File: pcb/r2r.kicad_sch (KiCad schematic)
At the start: 8 parts

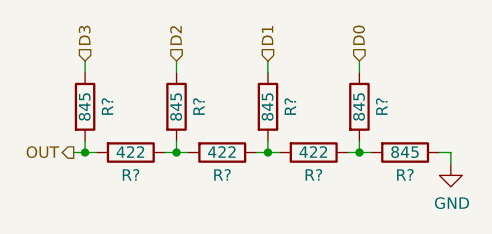
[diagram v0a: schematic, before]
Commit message: PCB: add reset circuit, xtal
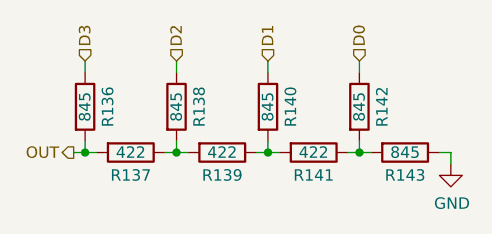
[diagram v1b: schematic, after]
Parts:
- gave numbers to parts that had none: 8
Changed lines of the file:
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@@
 (kicad_sch
-	(version 20231120)
+	(version 20250114)
 	(generator "eeschema")
-	(generator_version "8.0")
+	(generator_version "9.0")
 	(paper "A5")
 	(junction
@@
 		(on_board yes)
 		(dnp no)
-		(property "Reference" "#PWR?"
+		(property "Reference" "#PWR0413"
 			(at 127 71.12 0)
 			(effects
@@
 			(project "fnx51"
 				(path "/e63e39d7-6ac0-4ffd-8aa3-1841a4541b55/90e1f016-3c60-4383-aa8d-def9977ac47b/91068912-38bb-46cd-9b18-d1871085dfd0"
-					(reference "#PWR?")
+					(reference "#PWR0415")
 					(unit 1)
 				)
 				(path "/e63e39d7-6ac0-4ffd-8aa3-1841a4541b55/90e1f016-3c60-4383-aa8d-def9977ac47b/aa0b7daf-7acd-446b-bc05-f74af189bf7c"
-					(reference "#PWR?")
+					(reference "#PWR0414")
 					(unit 1)
 				)
 				(path "/e63e39d7-6ac0-4ffd-8aa3-1841a4541b55/90e1f016-3c60-4383-aa8d-def9977ac47b/dde75323-f81a-495f-a05e-373a126dd215"
-					(reference "#PWR?")
+					(reference "#PWR0413")
 					(unit 1)
 				)
@@
 		(on_board yes)
 		(dnp no)
-		(property "Reference" "R?"
+		(property "Reference" "R142"
 			(at 119.38 58.42 90)
 			(effects
@@
 			(project "fnx51"
 				(path "/e63e39d7-6ac0-4ffd-8aa3-1841a4541b55/90e1f016-3c60-4383-aa8d-def9977ac47b/91068912-38bb-46cd-9b18-d1871085dfd0"
-					(reference "R?")
+					(reference "R158")
 					(unit 1)
 				)
 				(path "/e63e39d7-6ac0-4ffd-8aa3-1841a4541b55/90e1f016-3c60-4383-aa8d-def9977ac47b/aa0b7daf-7acd-446b-bc05-f74af189bf7c"
-					(reference "R?")
+					(reference "R150")
 					(unit 1)
 				)
 				(path "/e63e39d7-6ac0-4ffd-8aa3-1841a4541b55/90e1f016-3c60-4383-aa8d-def9977ac47b/dde75323-f81a-495f-a05e-373a126dd215"
-					(reference "R?")
+					(reference "R142")
 					(unit 1)
 				)
@@
 		(on_board yes)
 		(dnp no)
-		(property "Reference" "R?"
+		(property "Reference" "R138"
 			(at 99.06 58.42 90)
 			(effects
@@
 			(project "fnx51"
 				(path "/e63e39d7-6ac0-4ffd-8aa3-1841a4541b55/90e1f016-3c60-4383-aa8d-def9977ac47b/91068912-38bb-46cd-9b18-d1871085dfd0"
-					(reference "R?")
+					(reference "R154")
 					(unit 1)
 				)
 				(path "/e63e39d7-6ac0-4ffd-8aa3-1841a4541b55/90e1f016-3c60-4383-aa8d-def9977ac47b/aa0b7daf-7acd-446b-bc05-f74af189bf7c"
-					(reference "R?")
+					(reference "R146")
 					(unit 1)
 				)
 				(path "/e63e39d7-6ac0-4ffd-8aa3-1841a4541b55/90e1f016-3c60-4383-aa8d-def9977ac47b/dde75323-f81a-495f-a05e-373a126dd215"
-					(reference "R?")
+					(reference "R138")
 					(unit 1)
 				)
@@
 		(on_board yes)
 		(dnp no)
-		(property "Reference" "R?"
+		(property "Reference" "R139"
 			(at 101.6 66.04 90)
 			(effects
@@
 			(project "fnx51"
 				(path "/e63e39d7-6ac0-4ffd-8aa3-1841a4541b55/90e1f016-3c60-4383-aa8d-def9977ac47b/91068912-38bb-46cd-9b18-d1871085dfd0"
-					(reference "R?")
+					(reference "R155")
 					(unit 1)
 				)
 				(path "/e63e39d7-6ac0-4ffd-8aa3-1841a4541b55/90e1f016-3c60-4383-aa8d-def9977ac47b/aa0b7daf-7acd-446b-bc05-f74af189bf7c"
-					(reference "R?")
+					(reference "R147")
 					(unit 1)
 				)
 				(path "/e63e39d7-6ac0-4ffd-8aa3-1841a4541b55/90e1f016-3c60-4383-aa8d-def9977ac47b/dde75323-f81a-495f-a05e-373a126dd215"
-					(reference "R?")
+					(reference "R139")
 					(unit 1)
 				)
@@
 		(on_board yes)
 		(dnp no)
-		(property "Reference" "R?"
+		(property "Reference" "R140"
 			(at 109.22 58.42 90)
 			(effects
@@
 			(project "fnx51"
 				(path "/e63e39d7-6ac0-4ffd-8aa3-1841a4541b55/90e1f016-3c60-4383-aa8d-def9977ac47b/91068912-38bb-46cd-9b18-d1871085dfd0"
-					(reference "R?")
+					(reference "R156")
 					(unit 1)
 				)
 				(path "/e63e39d7-6ac0-4ffd-8aa3-1841a4541b55/90e1f016-3c60-4383-aa8d-def9977ac47b/aa0b7daf-7acd-446b-bc05-f74af189bf7c"
-					(reference "R?")
+					(reference "R148")
 					(unit 1)
 				)
 				(path "/e63e39d7-6ac0-4ffd-8aa3-1841a4541b55/90e1f016-3c60-4383-aa8d-def9977ac47b/dde75323-f81a-495f-a05e-373a126dd215"
-					(reference "R?")
+					(reference "R140")
 					(unit 1)
 				)
@@
 		(on_board yes)
 		(dnp no)
-		(property "Reference" "R?"
+		(property "Reference" "R143"
 			(at 121.92 66.04 90)
 			(effects
@@
 			(project "fnx51"
 				(path "/e63e39d7-6ac0-4ffd-8aa3-1841a4541b55/90e1f016-3c60-4383-aa8d-def9977ac47b/91068912-38bb-46cd-9b18-d1871085dfd0"
-					(reference "R?")
+					(reference "R159")
 					(unit 1)
 				)
 				(path "/e63e39d7-6ac0-4ffd-8aa3-1841a4541b55/90e1f016-3c60-4383-aa8d-def9977ac47b/aa0b7daf-7acd-446b-bc05-f74af189bf7c"
-					(reference "R?")
+					(reference "R151")
 					(unit 1)
 				)
 				(path "/e63e39d7-6ac0-4ffd-8aa3-1841a4541b55/90e1f016-3c60-4383-aa8d-def9977ac47b/dde75323-f81a-495f-a05e-373a126dd215"
-					(reference "R?")
+					(reference "R143")
 					(unit 1)
 				)
@@
 		(on_board yes)
 		(dnp no)
-		(property "Reference" "R?"
+		(property "Reference" "R137"
 			(at 91.44 66.04 90)
 			(effects
@@
 			(project "fnx51"
 				(path "/e63e39d7-6ac0-4ffd-8aa3-1841a4541b55/90e1f016-3c60-4383-aa8d-def9977ac47b/91068912-38bb-46cd-9b18-d1871085dfd0"
-					(reference "R?")
+					(reference "R153")
 					(unit 1)
 				)
 				(path "/e63e39d7-6ac0-4ffd-8aa3-1841a4541b55/90e1f016-3c60-4383-aa8d-def9977ac47b/aa0b7daf-7acd-446b-bc05-f74af189bf7c"
-					(reference "R?")
+					(reference "R145")
 					(unit 1)
 				)
 				(path "/e63e39d7-6ac0-4ffd-8aa3-1841a4541b55/90e1f016-3c60-4383-aa8d-def9977ac47b/dde75323-f81a-495f-a05e-373a126dd215"
-					(reference "R?")
+					(reference "R137")
 					(unit 1)
 				)
@@
 		(on_board yes)
 		(dnp no)
-		(property "Reference" "R?"
+		(property "Reference" "R141"
 			(at 111.76 66.04 90)
 			(effects
@@
 			(project "fnx51"
 				(path "/e63e39d7-6ac0-4ffd-8aa3-1841a4541b55/90e1f016-3c60-4383-aa8d-def9977ac47b/91068912-38bb-46cd-9b18-d1871085dfd0"
-					(reference "R?")
+					(reference "R157")
 					(unit 1)
 				)
 				(path "/e63e39d7-6ac0-4ffd-8aa3-1841a4541b55/90e1f016-3c60-4383-aa8d-def9977ac47b/aa0b7daf-7acd-446b-bc05-f74af189bf7c"
-					(reference "R?")
+					(reference "R149")
 					(unit 1)
 				)
 				(path "/e63e39d7-6ac0-4ffd-8aa3-1841a4541b55/90e1f016-3c60-4383-aa8d-def9977ac47b/dde75323-f81a-495f-a05e-373a126dd215"
-					(reference "R?")
+					(reference "R141")
 					(unit 1)
 				)
@@
 		(on_board yes)
 		(dnp no)
-		(property "Reference" "R?"
+		(property "Reference" "R136"
 			(at 88.9 58.42 90)
 			(effects
@@
 			(project "fnx51"
 				(path "/e63e39d7-6ac0-4ffd-8aa3-1841a4541b55/90e1f016-3c60-4383-aa8d-def9977ac47b/91068912-38bb-46cd-9b18-d1871085dfd0"
-					(reference "R?")
+					(reference "R152")
 					(unit 1)
 				)
 				(path "/e63e39d7-6ac0-4ffd-8aa3-1841a4541b55/90e1f016-3c60-4383-aa8d-def9977ac47b/aa0b7daf-7acd-446b-bc05-f74af189bf7c"
-					(reference "R?")
+					(reference "R144")
 					(unit 1)
 				)
 				(path "/e63e39d7-6ac0-4ffd-8aa3-1841a4541b55/90e1f016-3c60-4383-aa8d-def9977ac47b/dde75323-f81a-495f-a05e-373a126dd215"
-					(reference "R?")
-					(unit 1)
-				)
+					(reference "R136")
+					(unit 1)
+				)

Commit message: WIP schematic
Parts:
- renumbered R136 to R143, R137 to R144, R138 to R145, R139 to R146, R140 to R147, R141 to R148, R142 to R149, R143 to R150
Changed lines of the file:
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@@
 		(on_board yes)
 		(dnp no)
-		(property "Reference" "#PWR0413"
+		(property "Reference" "#PWR0430"
 			(at 127 71.12 0)
 			(effects
@@
 			(project "fnx51"
 				(path "/e63e39d7-6ac0-4ffd-8aa3-1841a4541b55/90e1f016-3c60-4383-aa8d-def9977ac47b/91068912-38bb-46cd-9b18-d1871085dfd0"
-					(reference "#PWR0415")
-					(unit 1)
-				)
-				(path "/e63e39d7-6ac0-4ffd-8aa3-1841a4541b55/90e1f016-3c60-4383-aa8d-def9977ac47b/aa0b7daf-7acd-446b-bc05-f74af189bf7c"
-					(reference "#PWR0414")
-					(unit 1)
-				)
-				(path "/e63e39d7-6ac0-4ffd-8aa3-1841a4541b55/90e1f016-3c60-4383-aa8d-def9977ac47b/dde75323-f81a-495f-a05e-373a126dd215"
-					(reference "#PWR0413")
+					(reference "#PWR0432")
+					(unit 1)
+				)
+				(path "/e63e39d7-6ac0-4ffd-8aa3-1841a4541b55/90e1f016-3c60-4383-aa8d-def9977ac47b/aa0b7daf-7acd-446b-bc05-f74af189bf7c"
+					(reference "#PWR0431")
+					(unit 1)
+				)
+				(path "/e63e39d7-6ac0-4ffd-8aa3-1841a4541b55/90e1f016-3c60-4383-aa8d-def9977ac47b/dde75323-f81a-495f-a05e-373a126dd215"
+					(reference "#PWR0430")
 					(unit 1)
 				)
@@
 		(on_board yes)
 		(dnp no)
-		(property "Reference" "R142"
+		(property "Reference" "R149"
 			(at 119.38 58.42 90)
 			(effects
@@
 			(project "fnx51"
 				(path "/e63e39d7-6ac0-4ffd-8aa3-1841a4541b55/90e1f016-3c60-4383-aa8d-def9977ac47b/91068912-38bb-46cd-9b18-d1871085dfd0"
-					(reference "R158")
-					(unit 1)
-				)
-				(path "/e63e39d7-6ac0-4ffd-8aa3-1841a4541b55/90e1f016-3c60-4383-aa8d-def9977ac47b/aa0b7daf-7acd-446b-bc05-f74af189bf7c"
-					(reference "R150")
-					(unit 1)
-				)
-				(path "/e63e39d7-6ac0-4ffd-8aa3-1841a4541b55/90e1f016-3c60-4383-aa8d-def9977ac47b/dde75323-f81a-495f-a05e-373a126dd215"
-					(reference "R142")
+					(reference "R165")
+					(unit 1)
+				)
+				(path "/e63e39d7-6ac0-4ffd-8aa3-1841a4541b55/90e1f016-3c60-4383-aa8d-def9977ac47b/aa0b7daf-7acd-446b-bc05-f74af189bf7c"
+					(reference "R157")
+					(unit 1)
+				)
+				(path "/e63e39d7-6ac0-4ffd-8aa3-1841a4541b55/90e1f016-3c60-4383-aa8d-def9977ac47b/dde75323-f81a-495f-a05e-373a126dd215"
+					(reference "R149")
 					(unit 1)
 				)
@@
 		(on_board yes)
 		(dnp no)
-		(property "Reference" "R138"
+		(property "Reference" "R145"
 			(at 99.06 58.42 90)
 			(effects
@@
 			(project "fnx51"
 				(path "/e63e39d7-6ac0-4ffd-8aa3-1841a4541b55/90e1f016-3c60-4383-aa8d-def9977ac47b/91068912-38bb-46cd-9b18-d1871085dfd0"
-					(reference "R154")
-					(unit 1)
-				)
-				(path "/e63e39d7-6ac0-4ffd-8aa3-1841a4541b55/90e1f016-3c60-4383-aa8d-def9977ac47b/aa0b7daf-7acd-446b-bc05-f74af189bf7c"
-					(reference "R146")
-					(unit 1)
-				)
-				(path "/e63e39d7-6ac0-4ffd-8aa3-1841a4541b55/90e1f016-3c60-4383-aa8d-def9977ac47b/dde75323-f81a-495f-a05e-373a126dd215"
-					(reference "R138")
+					(reference "R161")
+					(unit 1)
+				)
+				(path "/e63e39d7-6ac0-4ffd-8aa3-1841a4541b55/90e1f016-3c60-4383-aa8d-def9977ac47b/aa0b7daf-7acd-446b-bc05-f74af189bf7c"
+					(reference "R153")
+					(unit 1)
+				)
+				(path "/e63e39d7-6ac0-4ffd-8aa3-1841a4541b55/90e1f016-3c60-4383-aa8d-def9977ac47b/dde75323-f81a-495f-a05e-373a126dd215"
+					(reference "R145")
 					(unit 1)
 				)
@@
 		(on_board yes)
 		(dnp no)
-		(property "Reference" "R139"
+		(property "Reference" "R146"
 			(at 101.6 66.04 90)
 			(effects
@@
 			(project "fnx51"
 				(path "/e63e39d7-6ac0-4ffd-8aa3-1841a4541b55/90e1f016-3c60-4383-aa8d-def9977ac47b/91068912-38bb-46cd-9b18-d1871085dfd0"
-					(reference "R155")
-					(unit 1)
-				)
-				(path "/e63e39d7-6ac0-4ffd-8aa3-1841a4541b55/90e1f016-3c60-4383-aa8d-def9977ac47b/aa0b7daf-7acd-446b-bc05-f74af189bf7c"
-					(reference "R147")
-					(unit 1)
-				)
-				(path "/e63e39d7-6ac0-4ffd-8aa3-1841a4541b55/90e1f016-3c60-4383-aa8d-def9977ac47b/dde75323-f81a-495f-a05e-373a126dd215"
-					(reference "R139")
+					(reference "R162")
+					(unit 1)
+				)
+				(path "/e63e39d7-6ac0-4ffd-8aa3-1841a4541b55/90e1f016-3c60-4383-aa8d-def9977ac47b/aa0b7daf-7acd-446b-bc05-f74af189bf7c"
+					(reference "R154")
+					(unit 1)
+				)
+				(path "/e63e39d7-6ac0-4ffd-8aa3-1841a4541b55/90e1f016-3c60-4383-aa8d-def9977ac47b/dde75323-f81a-495f-a05e-373a126dd215"
+					(reference "R146")
 					(unit 1)
 				)
@@
 		(on_board yes)
 		(dnp no)
-		(property "Reference" "R140"
+		(property "Reference" "R147"
 			(at 109.22 58.42 90)
 			(effects
@@
 			(project "fnx51"
 				(path "/e63e39d7-6ac0-4ffd-8aa3-1841a4541b55/90e1f016-3c60-4383-aa8d-def9977ac47b/91068912-38bb-46cd-9b18-d1871085dfd0"
-					(reference "R156")
-					(unit 1)
-				)
-				(path "/e63e39d7-6ac0-4ffd-8aa3-1841a4541b55/90e1f016-3c60-4383-aa8d-def9977ac47b/aa0b7daf-7acd-446b-bc05-f74af189bf7c"
-					(reference "R148")
-					(unit 1)
-				)
-				(path "/e63e39d7-6ac0-4ffd-8aa3-1841a4541b55/90e1f016-3c60-4383-aa8d-def9977ac47b/dde75323-f81a-495f-a05e-373a126dd215"
-					(reference "R140")
+					(reference "R163")
+					(unit 1)
+				)
+				(path "/e63e39d7-6ac0-4ffd-8aa3-1841a4541b55/90e1f016-3c60-4383-aa8d-def9977ac47b/aa0b7daf-7acd-446b-bc05-f74af189bf7c"
+					(reference "R155")
+					(unit 1)
+				)
+				(path "/e63e39d7-6ac0-4ffd-8aa3-1841a4541b55/90e1f016-3c60-4383-aa8d-def9977ac47b/dde75323-f81a-495f-a05e-373a126dd215"
+					(reference "R147")
 					(unit 1)
 				)
@@
 		(on_board yes)
 		(dnp no)
-		(property "Reference" "R143"
+		(property "Reference" "R150"
 			(at 121.92 66.04 90)
 			(effects
@@
 			(project "fnx51"
 				(path "/e63e39d7-6ac0-4ffd-8aa3-1841a4541b55/90e1f016-3c60-4383-aa8d-def9977ac47b/91068912-38bb-46cd-9b18-d1871085dfd0"
-					(reference "R159")
-					(unit 1)
-				)
-				(path "/e63e39d7-6ac0-4ffd-8aa3-1841a4541b55/90e1f016-3c60-4383-aa8d-def9977ac47b/aa0b7daf-7acd-446b-bc05-f74af189bf7c"
-					(reference "R151")
-					(unit 1)
-				)
-				(path "/e63e39d7-6ac0-4ffd-8aa3-1841a4541b55/90e1f016-3c60-4383-aa8d-def9977ac47b/dde75323-f81a-495f-a05e-373a126dd215"
-					(reference "R143")
+					(reference "R166")
+					(unit 1)
+				)
+				(path "/e63e39d7-6ac0-4ffd-8aa3-1841a4541b55/90e1f016-3c60-4383-aa8d-def9977ac47b/aa0b7daf-7acd-446b-bc05-f74af189bf7c"
+					(reference "R158")
+					(unit 1)
+				)
+				(path "/e63e39d7-6ac0-4ffd-8aa3-1841a4541b55/90e1f016-3c60-4383-aa8d-def9977ac47b/dde75323-f81a-495f-a05e-373a126dd215"
+					(reference "R150")
 					(unit 1)
 				)
@@
 		(on_board yes)
 		(dnp no)
-		(property "Reference" "R137"
+		(property "Reference" "R144"
 			(at 91.44 66.04 90)
 			(effects
@@
 			(project "fnx51"
 				(path "/e63e39d7-6ac0-4ffd-8aa3-1841a4541b55/90e1f016-3c60-4383-aa8d-def9977ac47b/91068912-38bb-46cd-9b18-d1871085dfd0"
-					(reference "R153")
-					(unit 1)
-				)
-				(path "/e63e39d7-6ac0-4ffd-8aa3-1841a4541b55/90e1f016-3c60-4383-aa8d-def9977ac47b/aa0b7daf-7acd-446b-bc05-f74af189bf7c"
-					(reference "R145")
-					(unit 1)
-				)
-				(path "/e63e39d7-6ac0-4ffd-8aa3-1841a4541b55/90e1f016-3c60-4383-aa8d-def9977ac47b/dde75323-f81a-495f-a05e-373a126dd215"
-					(reference "R137")
+					(reference "R160")
+					(unit 1)
+				)
+				(path "/e63e39d7-6ac0-4ffd-8aa3-1841a4541b55/90e1f016-3c60-4383-aa8d-def9977ac47b/aa0b7daf-7acd-446b-bc05-f74af189bf7c"
+					(reference "R152")
+					(unit 1)
+				)
+				(path "/e63e39d7-6ac0-4ffd-8aa3-1841a4541b55/90e1f016-3c60-4383-aa8d-def9977ac47b/dde75323-f81a-495f-a05e-373a126dd215"
+					(reference "R144")
 					(unit 1)
 				)
@@
 		(on_board yes)
 		(dnp no)
-		(property "Reference" "R141"
+		(property "Reference" "R148"
 			(at 111.76 66.04 90)
 			(effects
@@
 			(project "fnx51"
 				(path "/e63e39d7-6ac0-4ffd-8aa3-1841a4541b55/90e1f016-3c60-4383-aa8d-def9977ac47b/91068912-38bb-46cd-9b18-d1871085dfd0"
-					(reference "R157")
-					(unit 1)
-				)
-				(path "/e63e39d7-6ac0-4ffd-8aa3-1841a4541b55/90e1f016-3c60-4383-aa8d-def9977ac47b/aa0b7daf-7acd-446b-bc05-f74af189bf7c"
-					(reference "R149")
-					(unit 1)
-				)
-				(path "/e63e39d7-6ac0-4ffd-8aa3-1841a4541b55/90e1f016-3c60-4383-aa8d-def9977ac47b/dde75323-f81a-495f-a05e-373a126dd215"
-					(reference "R141")
+					(reference "R164")
+					(unit 1)
+				)
+				(path "/e63e39d7-6ac0-4ffd-8aa3-1841a4541b55/90e1f016-3c60-4383-aa8d-def9977ac47b/aa0b7daf-7acd-446b-bc05-f74af189bf7c"
+					(reference "R156")
+					(unit 1)
+				)
+				(path "/e63e39d7-6ac0-4ffd-8aa3-1841a4541b55/90e1f016-3c60-4383-aa8d-def9977ac47b/dde75323-f81a-495f-a05e-373a126dd215"
+					(reference "R148")
 					(unit 1)
 				)
@@
 		(on_board yes)
 		(dnp no)
-		(property "Reference" "R136"
+		(property "Reference" "R143"
 			(at 88.9 58.42 90)
 			(effects
@@
 			(project "fnx51"
 				(path "/e63e39d7-6ac0-4ffd-8aa3-1841a4541b55/90e1f016-3c60-4383-aa8d-def9977ac47b/91068912-38bb-46cd-9b18-d1871085dfd0"
-					(reference "R152")
-					(unit 1)
-				)
-				(path "/e63e39d7-6ac0-4ffd-8aa3-1841a4541b55/90e1f016-3c60-4383-aa8d-def9977ac47b/aa0b7daf-7acd-446b-bc05-f74af189bf7c"
-					(reference "R144")
-					(unit 1)
-				)
-				(path "/e63e39d7-6ac0-4ffd-8aa3-1841a4541b55/90e1f016-3c60-4383-aa8d-def9977ac47b/dde75323-f81a-495f-a05e-373a126dd215"
-					(reference "R136")
-					(unit 1)
-				)
+					(reference "R159")
+					(unit 1)
+				)
+				(path "/e63e39d7-6ac0-4ffd-8aa3-1841a4541b55/90e1f016-3c60-4383-aa8d-def9977ac47b/aa0b7daf-7acd-446b-bc05-f74af189bf7c"
+					(reference "R151")
+					(unit 1)
+				)
+				(path "/e63e39d7-6ac0-4ffd-8aa3-1841a4541b55/90e1f016-3c60-4383-aa8d-def9977ac47b/dde75323-f81a-495f-a05e-373a126dd215"
+					(reference "R143")
+					(unit 1)
+				)

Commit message: WIP schematic
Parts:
- renumbered R143 to R169, R144 to R170, R145 to R171, R146 to R172, R147 to R173, R148 to R174, R149 to R175, R150 to R176
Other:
- moved on the sheet: R169, R170, R171, R172, R173, R174, R175, R176
